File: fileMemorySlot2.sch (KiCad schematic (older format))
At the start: 4 parts, among them J13 MM1_addressExtension, J8 MM1_receptacle_5530843-2

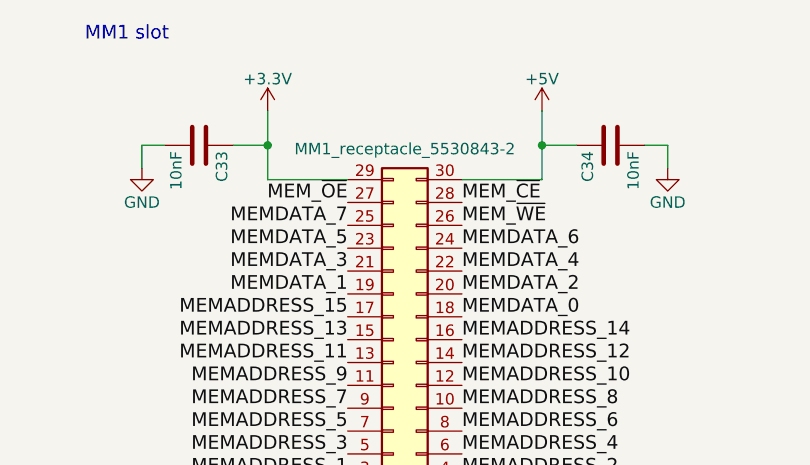
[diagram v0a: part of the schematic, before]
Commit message: V5.1 (#15)
* Remove compatibility for 5.0, 4.x and add 5.1+

* Fix switched pins on SN74LV393A #7

* Removed capacitor on 12V #11

* Add/Modify power decoupling capacitor #10

* Removing ADDSCR_CLK delay #9

* Schematics : set version 5.1, 2021 copyright and publish date

* Put non-electrolytic capacitor #10

* Set every capacitor size to 0805

* Add new footprint for J7 TE_3-641124-6 #6

* Schematic : set pinHeader on J12 #4

* Netlist, apply change to board, clean track, #6 #4 #12 #10

* Set version to 5.1, 2021 copyright and date, replace the missing QRcode

* Back the MM1 connectors #8

* Replace capacitor for U22 U23 U24 #13

* Better decoupling

* Increase version, year to 2021, clear status

* Precise the molex connector for power supply

* First step, import ses

* Clean bottom layer

* #14 Set the BWRITE2 bus instead of BWRITE1 on U12

* netlist, redo autorouting and cleaning

* use shields.io for colored badge

* Update gerbert files

* Changelog, updated BOM

* Small revision on blockDiagram

* Update README.md

* exporting pcb in pdf

* 3D images, diagram.png

* Update schematics pdf

* redo wavedrom_24bitsCounter
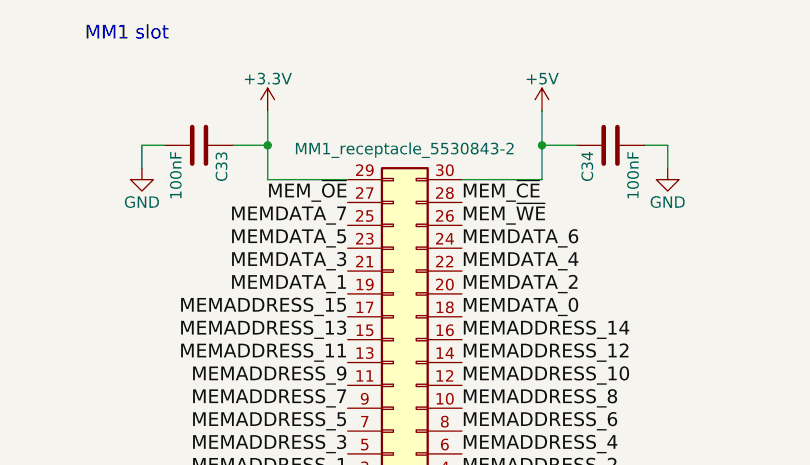
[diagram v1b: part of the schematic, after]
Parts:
- C26, C27: value 10nF -> 100nF
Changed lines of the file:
@@
 Sheet 10 10
 Title "GCM"
-Date "2020-11-23"
-Rev "V5.0"
+Date "2021-02-16"
+Rev "V5.1"
 Comp "Guillaume Guillet"
-Comment1 "Copyright Guillaume Guillet 2020"
+Comment1 "Copyright Guillaume Guillet 2021"
 Comment2 "Licensed under CERN-OHL-W v2 or later"
 Comment3 ""
@@
 AR Path="/5E0692F0/5BB77E95" Ref="C33"  Part="1"
 F 0 "C33" H 5275 1750 50  0000 L CNN
-F 1 "10nF" H 5275 1550 50  0000 L CNN
+F 1 "100nF" H 5275 1550 50  0000 L CNN
 F 2 "Capacitor_SMD:C_0805_2012Metric" H 5288 1500 50  0001 C CNN
 F 3 "" H 5250 1650 50  0001 C CNN
@@
 AR Path="/5E0692F0/5BB77E9C" Ref="C34"  Part="1"
 F 0 "C34" H 7075 1750 50  0000 L CNN
-F 1 "10nF" H 7075 1550 50  0000 L CNN
+F 1 "100nF" H 7075 1550 50  0000 L CNN
 F 2 "Capacitor_SMD:C_0805_2012Metric" H 7088 1500 50  0001 C CNN
 F 3 "" H 7050 1650 50  0001 C CNN
